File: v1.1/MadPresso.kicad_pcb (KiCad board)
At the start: 2 copper layers, 108 x 57.5 mm, 70 parts, among them J1 Conn_01x07, J2 Conn_01x03, J3 Conn_01x04, Q1 BSS84, Q3 BC847, Q4 BT138-600, Q5 2N7002, Q6 BT138-600, Q7 2N7002, Q8 BT138-600, Q9 2N7002, U1 LTV-356T, U2 WeMos_D1_mini, U3 TLP160G, U4 TLP160G, U5 TLP160G, U6 MID400, U7 MID400, U8 ADC101C021CIMK

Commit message: cleanups all over
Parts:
- added C11: DNP, Capacitor_SMD:C_0603_1608Metric_Pad1.08x0.95mm_HandSolder, F.Cu at (84.6, 35.7)
- added R31: 0R, Resistor_SMD:R_0603_1608Metric_Pad0.98x0.95mm_HandSolder, F.Cu at (85.1, 20.8)
- C1: footprint Capacitor_SMD:C_0603_1608Metric_Pad1.05x0.95mm_HandSolder -> Capacitor_SMD:C_0603_1608Metric_Pad1.08x0.95mm_HandSolder
- C10: renamed from C7; footprint Capacitor_SMD:C_0603_1608Metric_Pad1.05x0.95mm_HandSolder -> Capacitor_SMD:C_0603_1608Metric_Pad1.08x0.95mm_HandSolder
- C2: renamed from C3; footprint Capacitor_SMD:C_0603_1608Metric_Pad1.05x0.95mm_HandSolder -> Capacitor_SMD:C_0603_1608Metric_Pad1.08x0.95mm_HandSolder
- C4: renamed from C8; footprint Capacitor_SMD:C_0603_1608Metric_Pad1.05x0.95mm_HandSolder -> Capacitor_SMD:C_0603_1608Metric_Pad1.08x0.95mm_HandSolder
- C5: renamed from C9; footprint Capacitor_SMD:C_0603_1608Metric_Pad1.05x0.95mm_HandSolder -> Capacitor_SMD:C_0603_1608Metric_Pad1.08x0.95mm_HandSolder
- C6: renamed from C10; footprint Capacitor_SMD:C_0603_1608Metric_Pad1.05x0.95mm_HandSolder -> Capacitor_SMD:C_0603_1608Metric_Pad1.08x0.95mm_HandSolder
- C7: renamed from C5; footprint Capacitor_SMD:C_0603_1608Metric_Pad1.05x0.95mm_HandSolder -> Capacitor_SMD:C_0603_1608Metric_Pad1.08x0.95mm_HandSolder
- C9: renamed from C6; footprint Capacitor_SMD:C_0603_1608Metric_Pad1.05x0.95mm_HandSolder -> Capacitor_SMD:C_0603_1608Metric_Pad1.08x0.95mm_HandSolder
- F1: value 0.1A/250V -> 0.2A/250V
- R1: renamed from R3; footprint Resistor_SMD:R_1206_3216Metric_Pad1.42x1.75mm_HandSolder -> Resistor_SMD:R_1206_3216Metric_Pad1.30x1.75mm_HandSolder
- R10: renamed from R2; footprint Resistor_SMD:R_0603_1608Metric_Pad1.05x0.95mm_HandSolder -> Resistor_SMD:R_0603_1608Metric_Pad0.98x0.95mm_HandSolder
- R11: renamed from R31; footprint Resistor_SMD:R_0603_1608Metric_Pad1.05x0.95mm_HandSolder -> Resistor_SMD:R_0603_1608Metric_Pad0.98x0.95mm_HandSolder
- R12: renamed from R13; footprint Resistor_SMD:R_0603_1608Metric_Pad1.05x0.95mm_HandSolder -> Resistor_SMD:R_0603_1608Metric_Pad0.98x0.95mm_HandSolder
- R13: renamed from R27; footprint Resistor_SMD:R_1206_3216Metric_Pad1.42x1.75mm_HandSolder -> Resistor_SMD:R_1206_3216Metric_Pad1.30x1.75mm_HandSolder
- R14: renamed from R5; footprint Resistor_SMD:R_1206_3216Metric_Pad1.42x1.75mm_HandSolder -> Resistor_SMD:R_1206_3216Metric_Pad1.30x1.75mm_HandSolder
- R15: renamed from R28; footprint Resistor_SMD:R_0603_1608Metric_Pad1.05x0.95mm_HandSolder -> Resistor_SMD:R_0603_1608Metric_Pad0.98x0.95mm_HandSolder
- R16: renamed from R29; footprint Resistor_SMD:R_1206_3216Metric_Pad1.42x1.75mm_HandSolder -> Resistor_SMD:R_1206_3216Metric_Pad1.30x1.75mm_HandSolder
- R17: renamed from R6; footprint Resistor_SMD:R_1206_3216Metric_Pad1.42x1.75mm_HandSolder -> Resistor_SMD:R_1206_3216Metric_Pad1.30x1.75mm_HandSolder
- R18: renamed from R30; footprint Resistor_SMD:R_0603_1608Metric_Pad1.05x0.95mm_HandSolder -> Resistor_SMD:R_0603_1608Metric_Pad0.98x0.95mm_HandSolder
- R19: renamed from R15; footprint Resistor_SMD:R_1206_3216Metric_Pad1.42x1.75mm_HandSolder -> Resistor_SMD:R_1206_3216Metric_Pad1.30x1.75mm_HandSolder
- R2: renamed from R4; footprint Resistor_SMD:R_1206_3216Metric_Pad1.42x1.75mm_HandSolder -> Resistor_SMD:R_1206_3216Metric_Pad1.30x1.75mm_HandSolder
- R20: renamed from R16; footprint Resistor_SMD:R_0603_1608Metric_Pad1.05x0.95mm_HandSolder -> Resistor_SMD:R_0603_1608Metric_Pad0.98x0.95mm_HandSolder
- R21: renamed from R17; footprint Resistor_SMD:R_0603_1608Metric_Pad1.05x0.95mm_HandSolder -> Resistor_SMD:R_0603_1608Metric_Pad0.98x0.95mm_HandSolder
- R22: renamed from R18; footprint Resistor_SMD:R_0603_1608Metric_Pad1.05x0.95mm_HandSolder -> Resistor_SMD:R_0603_1608Metric_Pad0.98x0.95mm_HandSolder
- R23: renamed from R19; footprint Resistor_SMD:R_1206_3216Metric_Pad1.42x1.75mm_HandSolder -> Resistor_SMD:R_1206_3216Metric_Pad1.30x1.75mm_HandSolder
- R24: renamed from R20; footprint Resistor_SMD:R_0603_1608Metric_Pad1.05x0.95mm_HandSolder -> Resistor_SMD:R_0603_1608Metric_Pad0.98x0.95mm_HandSolder
- R25: renamed from R21; footprint Resistor_SMD:R_0603_1608Metric_Pad1.05x0.95mm_HandSolder -> Resistor_SMD:R_0603_1608Metric_Pad0.98x0.95mm_HandSolder
- R26: renamed from R22; footprint Resistor_SMD:R_0603_1608Metric_Pad1.05x0.95mm_HandSolder -> Resistor_SMD:R_0603_1608Metric_Pad0.98x0.95mm_HandSolder
- R27: renamed from R23; footprint Resistor_SMD:R_1206_3216Metric_Pad1.42x1.75mm_HandSolder -> Resistor_SMD:R_1206_3216Metric_Pad1.30x1.75mm_HandSolder
- R28: renamed from R24; footprint Resistor_SMD:R_0603_1608Metric_Pad1.05x0.95mm_HandSolder -> Resistor_SMD:R_0603_1608Metric_Pad0.98x0.95mm_HandSolder
- R29: renamed from R25; footprint Resistor_SMD:R_0603_1608Metric_Pad1.05x0.95mm_HandSolder -> Resistor_SMD:R_0603_1608Metric_Pad0.98x0.95mm_HandSolder
- R3: renamed from R7; footprint Resistor_SMD:R_0603_1608Metric_Pad1.05x0.95mm_HandSolder -> Resistor_SMD:R_0603_1608Metric_Pad0.98x0.95mm_HandSolder
- R30: renamed from R26; footprint Resistor_SMD:R_0603_1608Metric_Pad1.05x0.95mm_HandSolder -> Resistor_SMD:R_0603_1608Metric_Pad0.98x0.95mm_HandSolder
- R4: renamed from R9; footprint Resistor_SMD:R_0603_1608Metric_Pad1.05x0.95mm_HandSolder -> Resistor_SMD:R_0603_1608Metric_Pad0.98x0.95mm_HandSolder
- R5: renamed from R11; footprint Resistor_SMD:R_0603_1608Metric_Pad1.05x0.95mm_HandSolder -> Resistor_SMD:R_0603_1608Metric_Pad0.98x0.95mm_HandSolder
- R6: renamed from R12; footprint Resistor_SMD:R_0603_1608Metric_Pad1.05x0.95mm_HandSolder -> Resistor_SMD:R_0603_1608Metric_Pad0.98x0.95mm_HandSolder
- R7: renamed from R14; footprint Resistor_SMD:R_0603_1608Metric_Pad1.05x0.95mm_HandSolder -> Resistor_SMD:R_0603_1608Metric_Pad0.98x0.95mm_HandSolder
- R8: footprint Resistor_SMD:R_0603_1608Metric_Pad1.05x0.95mm_HandSolder -> Resistor_SMD:R_0603_1608Metric_Pad0.98x0.95mm_HandSolder
- R9: renamed from R1; footprint Resistor_SMD:R_0603_1608Metric_Pad1.05x0.95mm_HandSolder -> Resistor_SMD:R_0603_1608Metric_Pad0.98x0.95mm_HandSolder
- U2: renamed from U8; footprint Package_TO_SOT_SMD:SOT-23-6 -> Package_TO_SOT_SMD:SOT-23-6_Handsoldering
- moved R18 15.0 mm to (91.4, 21.2), turned to 90 degrees
- moved R15 1.22 mm to (88.9, 36.7)
- moved REF** 1.13 mm to (101.5, 30.7)
- moved R4 0.80 mm to (79.2, 10.7)
- moved R2 0.31 mm to (19.6, 17.0)
- moved U2 0.29 mm to (82.7, 13.2)
- moved C6 0.14 mm to (86.6, 10.1)
- renumbered C2 to C3, C4 to C8, D6 to D2, D9 to D3, D2 to D4, D8 to D5, Q3 to Q1, Q1 to Q2, Q4 to Q3, Q5 to Q4, Q6 to Q5, Q7 to Q6, Q8 to Q7, Q9 to Q8, U2 to U3, U6 to U4, U7 to U5, U3 to U6, U4 to U7, U5 to U8
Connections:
- U2 pad 4: GND -> Net-(U2-Pad4)
- U3 pad 12: /PUMP_TRIAC -> /STEAM_SENSOR
- U3 pad 6: /STEAM_SENSOR -> /PUMP_TRIAC
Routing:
- net VCC: track 94.4 -> 112.4 mm
- net /STEAM_SENSOR: track 40.4 -> 26.7 mm, vias 1 -> 0
- net Net-(U2-Pad4): track 0.00 -> 7.29 mm
- net /HEATER_TRIAC: track 28.0 -> 31.3 mm
- net /SHOT_SENSOR: track 50.2 -> 52.9 mm, vias 0 -> 3
- net GND: track 91.2 -> 93.9 mm, vias 13 -> 16
- net /PUMP_TRIAC: track 24.2 -> 22.2 mm, vias 2 -> 1
- net /ADC: track 34.7 -> 32.9 mm, vias 1 -> 2
- net /TEMP_SENSOR: track 7.10 -> 8.19 mm

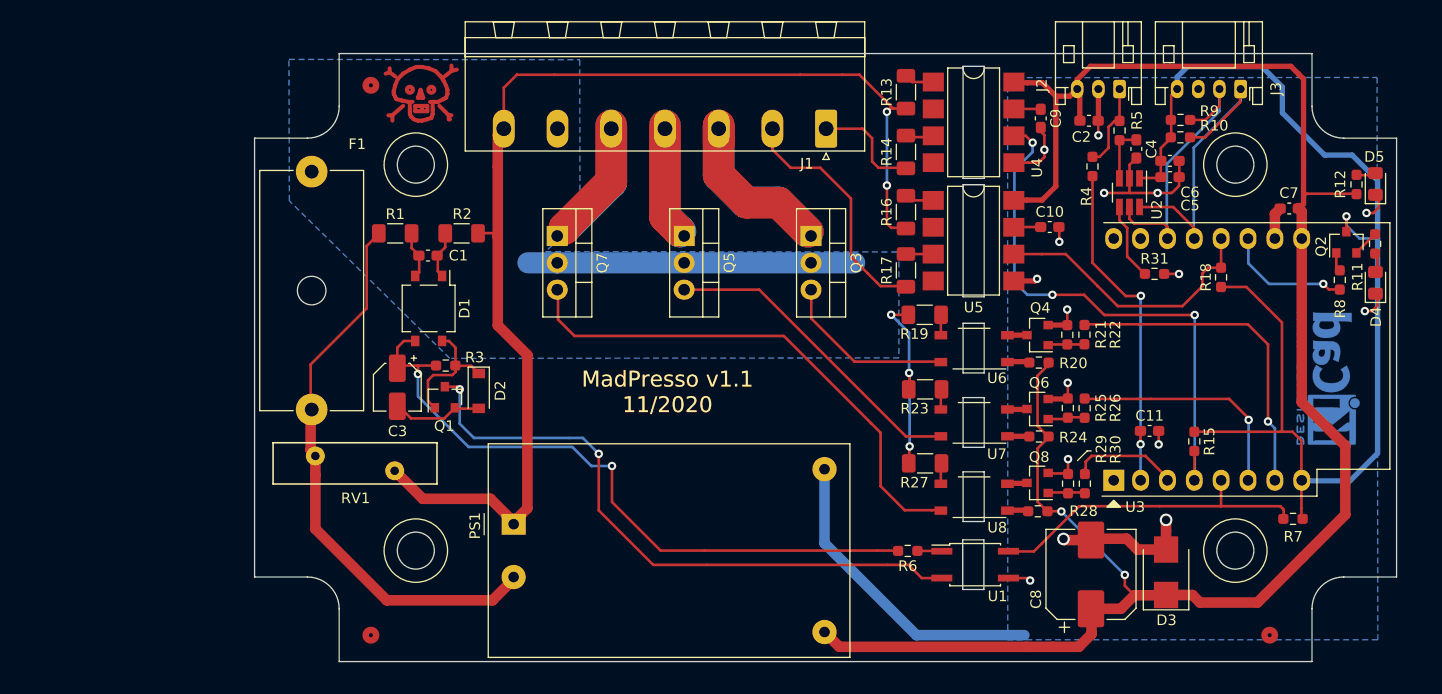
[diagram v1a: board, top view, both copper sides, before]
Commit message: start rework to smd triac
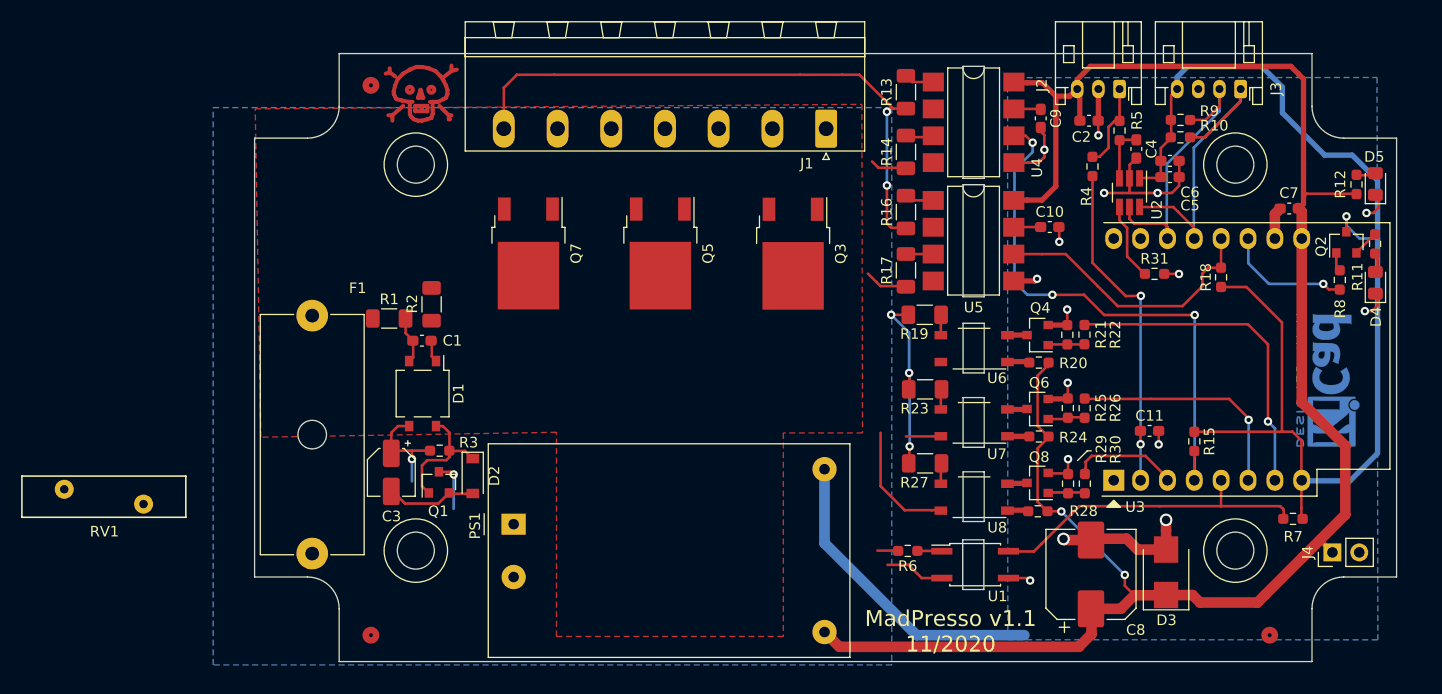
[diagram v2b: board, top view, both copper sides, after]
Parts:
- added J4: Conn_01x02, Connector_PinHeader_2.54mm:PinHeader_1x02_P2.54mm_Vertical, F.Cu at (101.9, 47.2)
- Q3, Q5, Q7: footprint Package_TO_SOT_THT:TO-220-3_Vertical -> Package_TO_SOT_SMD:TO-252-2
- moved RV1 24.0 mm to (-10.5, 42.6)
- moved F1 13.6 mm to (5.45, 24.8)
- moved D2 8.07 mm to (20.6, 40.0)
- moved C3 8.07 mm to (12.9, 39.6)
- moved R1 8.07 mm to (12.7, 25.1)
- moved C1 8.07 mm to (15.8, 27.1)
- moved D1 8.07 mm to (15.9, 32.1)
- moved Q1 8.07 mm to (17.4, 40.5)
- moved R3 8.07 mm to (17.5, 37.5)
- moved R2 7.29 mm to (16.7, 23.7), turned to -90 degrees
- moved Q7 3.19 mm to (25.9, 18.9)
- moved Q5 2.79 mm to (38.4, 18.9)
- moved Q3 2.38 mm to (50.9, 18.9)
- moved REF** 0.18 mm to (101.5, 30.9)
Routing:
- net NEUT: track 112.9 -> 57.0 mm
- net /LINE_FUSED: track 53.2 -> 0.00 mm
- net Net-(C3-Pad1): track 64.0 -> 12.8 mm, vias 2 -> 1
- net Net-(Q1-Pad3): track 59.8 -> 10.7 mm, vias 2 -> 1
- net Net-(Q7-Pad3): track 49.6 -> 11.7 mm
- net /HEATER: track 33.2 -> 0.00 mm
- net LINE: track 48.9 -> 18.0 mm
- net Net-(Q5-Pad3): track 30.1 -> 3.30 mm
- net /VALVE: track 25.0 -> 0.00 mm
- net /PUMP: track 21.2 -> 0.00 mm
- net /STEAM_SW: track 23.8 -> 4.09 mm
- net Net-(Q3-Pad3): track 16.6 -> 0.00 mm
- net /SHOT_SW: track 10.9 -> 3.45 mm
- net Net-(D1-Pad1): track 4.68 -> 2.25 mm
- net +5V: track 181.3 -> 183.0 mm
- added copper zone on F.Cu, net LINE

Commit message: more work on smd triac routing
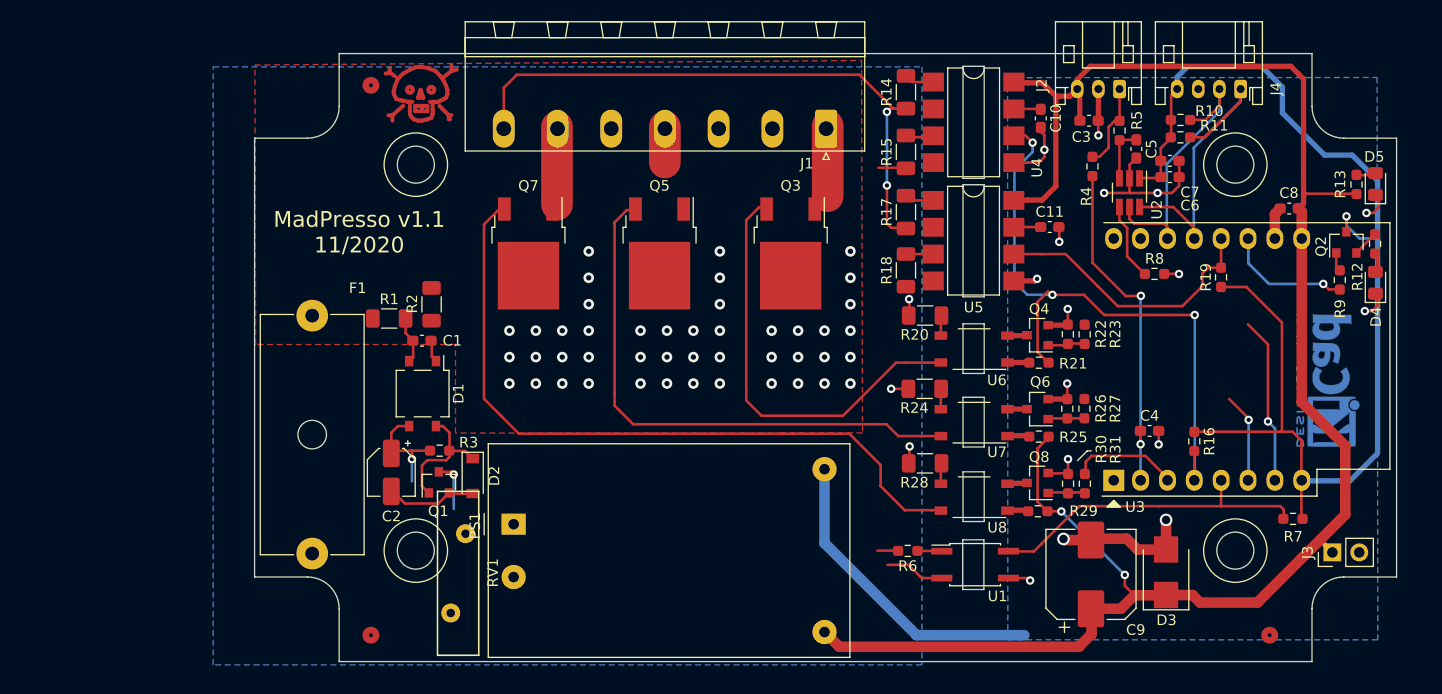
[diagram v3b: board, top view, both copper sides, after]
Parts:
- Q3: renamed from Q5; value BT138-600 -> T835-600B
- Q5: renamed from Q3; value BT138-600 -> T835-600B
- Q7: value BT138-600 -> T835-600B
- moved RV1 30.6 mm to (19.9, 45.4), turned to -90 degrees
- moved Q5 12.6 mm to (38.3, 18.9)
- moved Q3 12.3 mm to (50.7, 18.9)
- moved R26 7.00 mm to (76.9, 33.6)
- moved R27 7.00 mm to (78.5, 33.6)
- moved R24 7.00 mm to (63.4, 31.7)
- moved R25 7.00 mm to (74.2, 36.2)
- moved U7 7.00 mm to (68.0, 34.9)
- moved Q6 7.00 mm to (74.0, 33.6)
- moved R22 6.98 mm to (76.9, 26.5)
- moved Q4 6.98 mm to (74.0, 26.6)
- moved R20 6.98 mm to (63.4, 24.8)
- moved R21 6.98 mm to (74.2, 29.2)
- moved R23 6.98 mm to (78.5, 26.6)
- moved U6 6.98 mm to (68.0, 27.9)
- renumbered C9 to C10, C10 to C11, C3 to C2, C2 to C3, C11 to C4, C4 to C5, C5 to C6, C6 to C7, C7 to C8, C8 to C9, J4 to J3, J3 to J4, Q6 to Q4, Q4 to Q6, R9 to R10, R10 to R11, R11 to R12, R12 to R13, R13 to R14, R14 to R15, R15 to R16, R16 to R17, R17 to R18, R18 to R19, R23 to R20, R24 to R21, R25 to R22, R26 to R23, R19 to R24, R20 to R25, R21 to R26, R22 to R27, R27 to R28, R28 to R29, R29 to R30, R30 to R31, R31 to R8, R8 to R9, U7 to U6, U6 to U7
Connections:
- J1 pad 1: /SHOT_SW -> /PUMP
- J1 pad 2: /STEAM_SW -> /SHOT_SW
- J1 pad 3: /HEATER -> /STEAM_SW
- J1 pad 4: /PUMP -> /HEATER
- J1 pad 5: /VALVE -> LINE
- J1 pad 6: LINE -> /VALVE
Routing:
- net Net-(Q7-Pad3): track 11.7 -> 67.9 mm
- net Net-(Q5-Pad3): track 0.00 -> 52.0 mm
- net Net-(Q3-Pad3): track 3.30 -> 40.7 mm
- net /HEATER_TRIAC: track 31.3 -> 16.0 mm
- net /PUMP_TRIAC: track 22.2 -> 8.53 mm
- net LINE: track 18.0 -> 4.93 mm, vias 3 -> 48
- net /VALVE: track 0.00 -> 7.38 mm
- net /PUMP: track 0.00 -> 6.68 mm
- net /STEAM_SW: track 4.09 -> 0.00 mm
- net /HEATER: track 0.00 -> 3.40 mm
- net /SHOT_SW: track 3.45 -> 2.60 mm

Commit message: more routing
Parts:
- removed the REF** at (15.7, 3.80)
- added FID1: Fiducial, Fiducial:Fiducial_0.5mm_Mask1mm, F.Cu at (10.5, 2.40)
- added FID2: Fiducial, Fiducial:Fiducial_0.5mm_Mask1mm, F.Cu at (10.5, 55.0)
- added FID3: Fiducial, Fiducial:Fiducial_0.5mm_Mask1mm, F.Cu at (97.3, 55.0)
- added REF**: OSHW-Logo2_7.3x6mm_SilkScreen, Symbol:OSHW-Logo2_7.3x6mm_SilkScreen, F.Cu at (92.8, 53.7)
- moved F1 14.1 mm to (5.45, 10.7)
- moved R17 11.2 mm to (61.6, 3.79)
- moved U5 11.2 mm to (68.0, 6.49)
- moved C10 11.2 mm to (74.3, 17.3)
- moved R14 11.2 mm to (61.6, 14.8)
- moved R15 11.2 mm to (61.6, 20.5)
- moved R18 11.2 mm to (61.6, 9.30)
- moved U4 11.2 mm to (68.0, 17.7)
- moved C11 10.3 mm to (74.3, 6.10), turned to -90 degrees
- moved PS1 2.00 mm to (26.5, 44.5)
- moved Q3 1.95 mm to (50.7, 16.9)
- moved Q5 1.95 mm to (38.3, 16.9)
- moved Q7 1.95 mm to (25.9, 16.9)
- moved RV1 1.66 mm to (21.6, 45.6)
- moved R2 0.46 mm to (17.2, 23.7)
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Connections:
- J1 pad 4: /HEATER -> /VALVE
- J1 pad 6: /VALVE -> /HEATER
- Q5 pad 1: /HEATER -> /VALVE
- Q7 pad 1: /VALVE -> /HEATER
- R27 pad 1: /HEATER_TRIAC -> /VALVE_TRIAC
- R31 pad 1: /VALVE_TRIAC -> /HEATER_TRIAC
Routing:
- net NEUT: track 57.0 -> 140.9 mm, vias 2 -> 3
- net /LINE_FUSED: track 0.00 -> 50.1 mm
- net Net-(C2-Pad1): track 12.8 -> 60.2 mm, vias 1 -> 0
- net Net-(Q1-Pad3): track 10.7 -> 50.6 mm, vias 1 -> 0
- net /SHOT_SW: track 2.60 -> 30.9 mm
- net /STEAM_SW: track 0.00 -> 27.0 mm
- net /PUMP_TRIAC: track 8.53 -> 29.5 mm
- net /SHOT_SENSOR: track 52.9 -> 38.1 mm, vias 3 -> 1
- net /HEATER_TRIAC: track 16.0 -> 27.2 mm
- net /STEAM_SENSOR: track 26.7 -> 36.7 mm, vias 0 -> 2
- net Net-(Q7-Pad3): track 67.9 -> 74.8 mm
- net /VALVE_TRIAC: track 10.7 -> 16.4 mm, vias 0 -> 1
- net Net-(Q3-Pad3): track 40.7 -> 44.4 mm
- net Net-(D1-Pad4): track 12.3 -> 8.87 mm
- net /HEATER: track 3.40 -> 5.64 mm
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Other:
- board text added: "MadPresso v1.1"
- board text removed: "MadPresso v1.1 11/2020"

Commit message: more routing
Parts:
- removed the REF** at (92.8, 53.7)
- R14, R17: value 22k -> 22k/0.5W
- R15, R18: value 33k -> 33k/0.5W
- R20, R24, R28: value 1k -> 360R/0.5W
- R21, R25, R29: value 120 -> 360R
- R8: value 0R -> DNP
- moved REF** 0.39 mm to (101.5, 30.5)
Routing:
- net Net-(Q7-Pad3): track 74.8 -> 73.7 mm
- net Net-(Q5-Pad3): track 54.0 -> 53.4 mm
